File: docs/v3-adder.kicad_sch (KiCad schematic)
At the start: 102 parts, among them J1 Thonkiconn, J2 Thonkiconn, J3 Thonkiconn, J4 Thonkiconn, J5 Thonkiconn, J6 Thonkiconn, J7 Thonkiconn, J8 Thonkiconn, P1 Eurorack 2x5, SW1A SUBMINI ON-OFF-ON, SW1B SUBMINI ON-ON, SW2A SUBMINI ON-OFF-ON, SW2B SUBMINI ON-ON-ON, SW3A SUBMINI ON-OFF-ON, SW3B SUBMINI ON-ON-ON, SW4A SUBMINI ON-OFF-ON, SW4B SUBMINI ON-ON-ON, U1 OPA4196, U2 OPA4196, U3 OPA4196, U4 L78L05, U5 L79L05

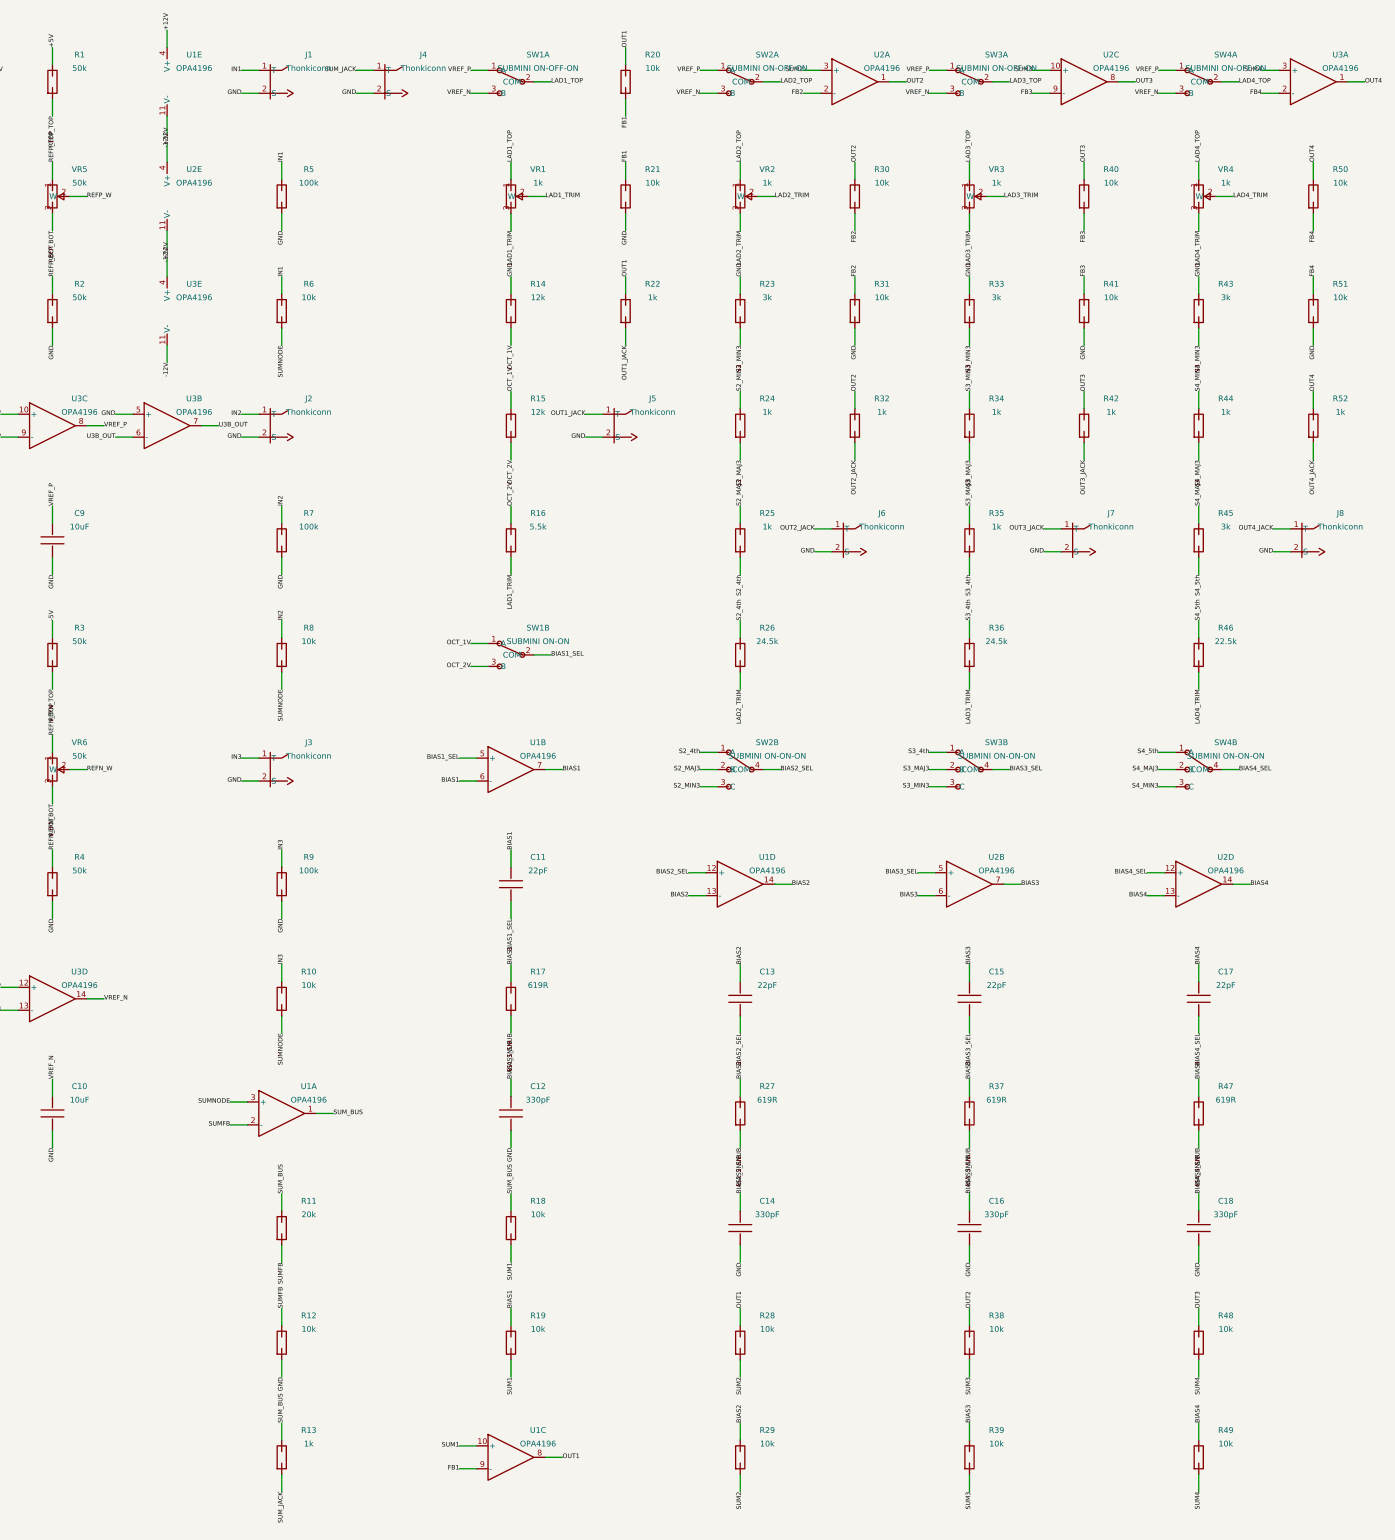
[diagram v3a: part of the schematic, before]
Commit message: Schematic: fix three functional defects found reviewing it
Asked to verify the schematic does what v3 needs before layout. The structure
was right - three summed inputs to SUM, four cascaded stages of polarity switch
plus tap selector plus buffer plus gain-2 adder, no leftover v2.2 passthru
buffers - but three things were wrong.

1. Unpatched inputs did not sum to zero. Each input jack had a 100k pulldown,
   which puts 110k rather than a driven 0 V on that leg of the passive
   averager. With one input patched - the normal case - the summer's gain was
   2.538 instead of 1.0, so a 1V/oct signal came out transposed by over an
   octave and a half. Fixed by wiring the Thonkiconn's own switch contact to
   GND, which grounds an unused tip properly; the pulldowns are gone.

2. No local decoupling on the op-amp packages. Only bulk caps at the power
   entry and the regulators. Added 0.1uF per rail per package, as v2.2 has.

3. A 22pF cap sat between each bias buffer's output and its + input, which is
   positive feedback around a follower. That was mine, not inherited: v2.2 puts
   its 22pF across the follower's feedback, and since that feedback is a plain
   wire the cap does nothing at all. Removed rather than reproduced.

check_function() now asserts the properties behind all three, plus the summing
ratios and the gain networks - things a connectivity check cannot see, because
a wrong value still connects. Verified against injected faults.

Still open before layout: the ON-ON-ON selectors are drawn as an ideal 1P3T,
but the physical part is a six-pin DPDT whose three positions come from
combining poles, and Type 1 and Type 2 differ. Symbol, footprint and tap wiring
all follow from which variant is bought.

ERC still 0 errors, 23 footprint warnings on the custom parts.

Co-Authored-By: Claude Opus 5 <noreply@anthropic.com>
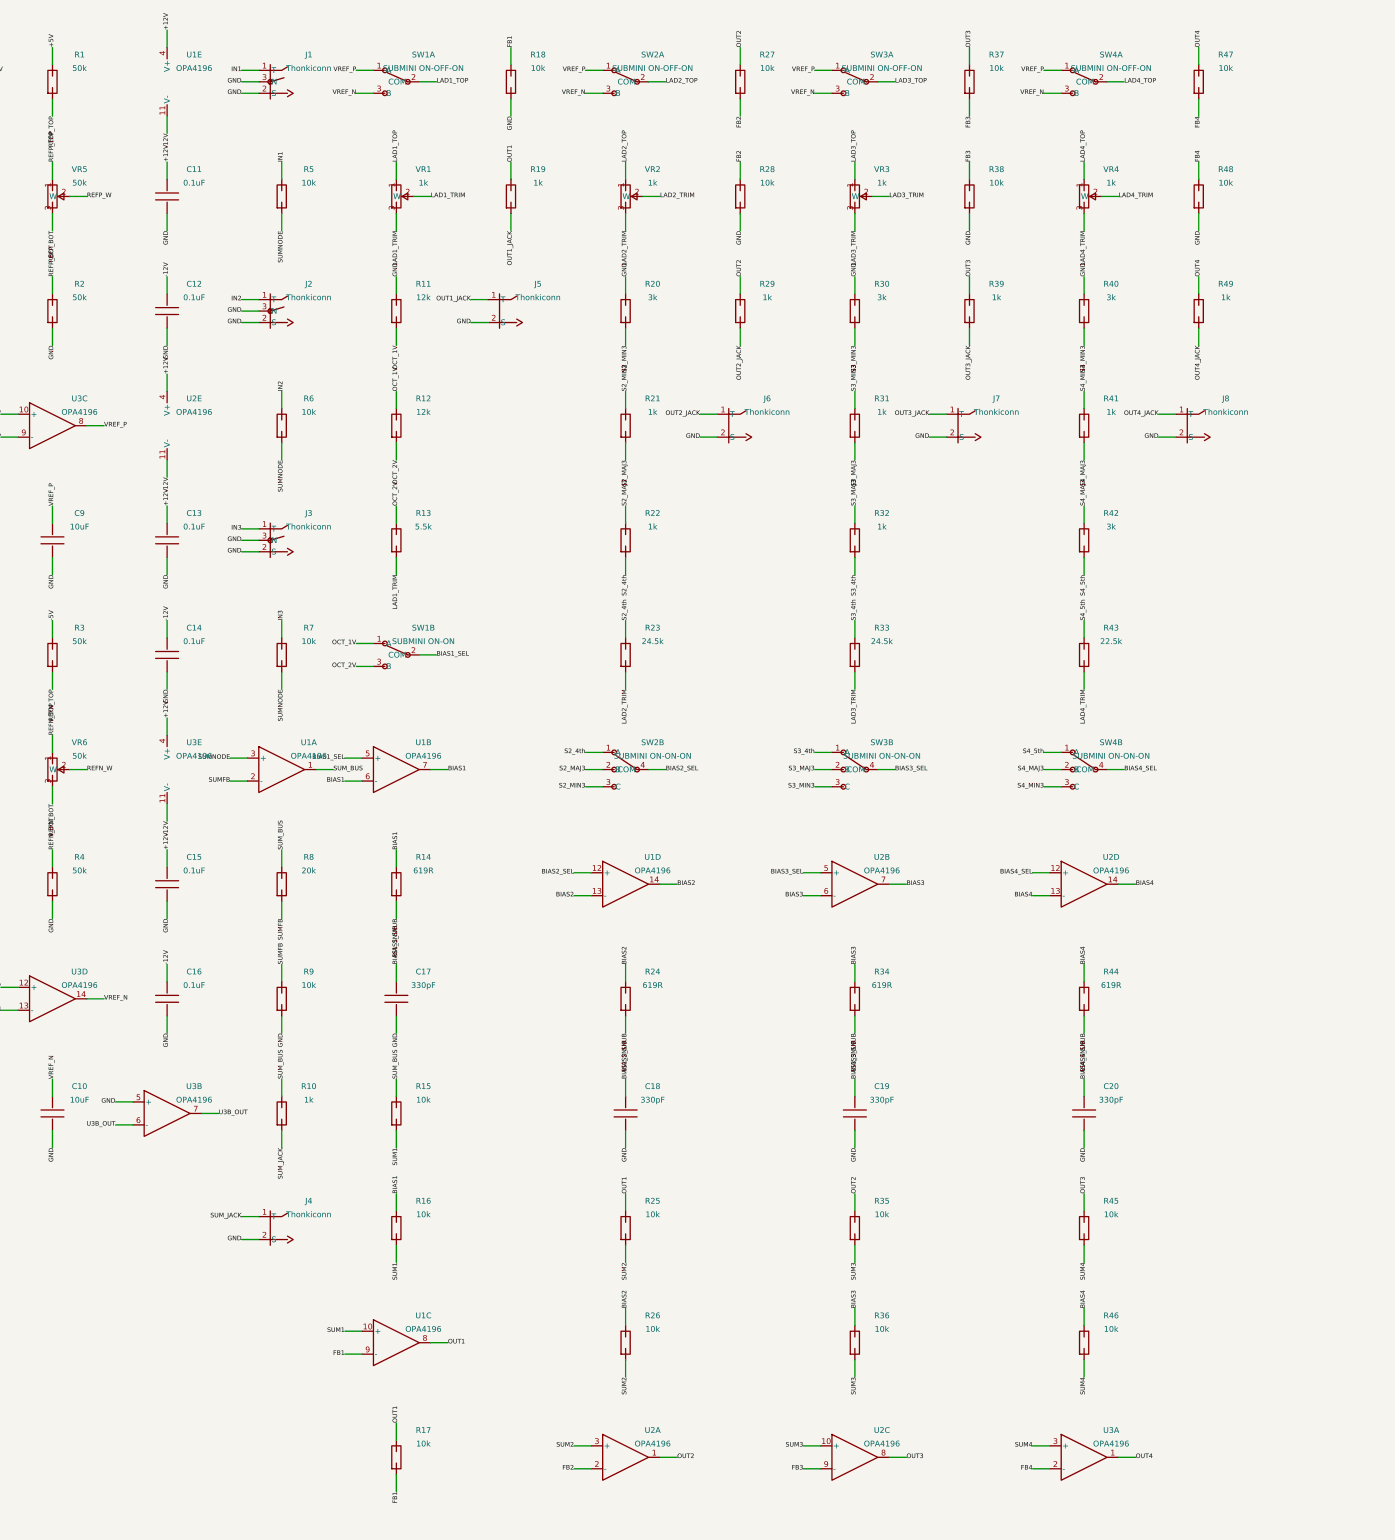
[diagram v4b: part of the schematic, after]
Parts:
- removed C11, C17: 22pF, Capacitor_SMD:C_0805_2012Metric, symbol adder:C
- removed C12: 330pF, Capacitor_SMD:C_0805_2012Metric, symbol adder:C
- removed J1, J2: Thonkiconn, THONKICONN-TIGHT, symbol adder:JACK
- removed R14: 12k, Resistor_SMD:R_0805_2012Metric, symbol adder:R
- removed R17, R27, R37: 619R, Resistor_SMD:R_0805_2012Metric, symbol adder:R
- removed R18, R20, R21, R30, R31, R40, R8: 10k, Resistor_SMD:R_0805_2012Metric, symbol adder:R
- removed R24, R25, R34: 1k, Resistor_SMD:R_0805_2012Metric, symbol adder:R
- removed R43: 3k, Resistor_SMD:R_0805_2012Metric, symbol adder:R
- added C13, C16: 0.1uF, Capacitor_SMD:C_0805_2012Metric, symbol adder:C
- added J2, J3: Thonkiconn, THONKICONN-TIGHT, symbol adder:JACK_SW
- added J5, J6: Thonkiconn, THONKICONN-TIGHT, symbol adder:JACK
- added R19: 1k, Resistor_SMD:R_0805_2012Metric, symbol adder:R
- added R26: 10k, Resistor_SMD:R_0805_2012Metric, symbol adder:R
- added SW1A, SW2A, SW3A, SW4A: SUBMINI ON-OFF-ON, SUBMINI_TOGGLE, symbol adder:SW_ONOFFON
- added SW3B, SW4B: SUBMINI ON-ON-ON, SUBMINI_TOGGLE, symbol adder:SW_1P3T
- added unit 3 of U1
- added unit 1 of U2
- added unit 3 of U2
- added unit 5 of U3
- added unit 2 of U3
- C11: renamed from U2; value OPA4196 -> 0.1uF; footprint Package_SO:SOIC-14_3.9x8.7mm_P1.27mm -> Capacitor_SMD:C_0805_2012Metric; symbol adder:OPA4196 -> adder:C
- C12: renamed from U3; value OPA4196 -> 0.1uF; footprint Package_SO:SOIC-14_3.9x8.7mm_P1.27mm -> Capacitor_SMD:C_0805_2012Metric; symbol adder:OPA4196 -> adder:C
- C14: value 330pF -> 0.1uF
- C15: value 22pF -> 0.1uF
- C17: renamed from U1; value OPA4196 -> 330pF; footprint Package_SO:SOIC-14_3.9x8.7mm_P1.27mm -> Capacitor_SMD:C_0805_2012Metric; symbol adder:OPA4196 -> adder:C
- C18: renamed from R29; value 10k -> 330pF; footprint Resistor_SMD:R_0805_2012Metric -> Capacitor_SMD:C_0805_2012Metric; symbol adder:R -> adder:C
- C19: renamed from R38; value 10k -> 330pF; footprint Resistor_SMD:R_0805_2012Metric -> Capacitor_SMD:C_0805_2012Metric; symbol adder:R -> adder:C
- J1: renamed from J3; symbol adder:JACK -> adder:JACK_SW
- J7: renamed from SW4A; value SUBMINI ON-OFF-ON -> Thonkiconn; footprint SUBMINI_TOGGLE -> THONKICONN-TIGHT; symbol adder:SW_ONOFFON -> adder:JACK
- R10: value 10k -> 1k
- R11: value 20k -> 12k
- R12: value 10k -> 12k
- R13: value 1k -> 5.5k
- R14: renamed from R19; value 10k -> 619R
- R15: value 12k -> 10k
- R16: value 5.5k -> 10k
- R17: renamed from J5; value Thonkiconn -> 10k; footprint THONKICONN-TIGHT -> Resistor_SMD:R_0805_2012Metric; symbol adder:JACK -> adder:R
- R18: renamed from SW2A; value SUBMINI ON-OFF-ON -> 10k; footprint SUBMINI_TOGGLE -> Resistor_SMD:R_0805_2012Metric; symbol adder:SW_ONOFFON -> adder:R
- R20: renamed from R26; value 24.5k -> 3k
- R21: renamed from SW2B; value SUBMINI ON-ON-ON -> 1k; footprint SUBMINI_TOGGLE -> Resistor_SMD:R_0805_2012Metric; symbol adder:SW_1P3T -> adder:R
- R23, R33: value 3k -> 24.5k
- R24: renamed from R28; value 10k -> 619R
- R25, R36: renamed from U2; value OPA4196 -> 10k; footprint Package_SO:SOIC-14_3.9x8.7mm_P1.27mm -> Resistor_SMD:R_0805_2012Metric; symbol adder:OPA4196 -> adder:R
- R27: renamed from R32; value 1k -> 10k
- R28: renamed from J6; value Thonkiconn -> 10k; footprint THONKICONN-TIGHT -> Resistor_SMD:R_0805_2012Metric; symbol adder:JACK -> adder:R
- R29: renamed from SW3A; value SUBMINI ON-OFF-ON -> 1k; footprint SUBMINI_TOGGLE -> Resistor_SMD:R_0805_2012Metric; symbol adder:SW_ONOFFON -> adder:R
- R30: renamed from R35; value 1k -> 3k
- R31: renamed from R36; value 24.5k -> 1k
- R32: renamed from SW3B; value SUBMINI ON-ON-ON -> 1k; footprint SUBMINI_TOGGLE -> Resistor_SMD:R_0805_2012Metric; symbol adder:SW_1P3T -> adder:R
- R34: renamed from C16; value 330pF -> 619R; footprint Capacitor_SMD:C_0805_2012Metric -> Resistor_SMD:R_0805_2012Metric; symbol adder:C -> adder:R
- R38: renamed from R42; value 1k -> 10k
- R39: renamed from J7; value Thonkiconn -> 1k; footprint THONKICONN-TIGHT -> Resistor_SMD:R_0805_2012Metric; symbol adder:JACK -> adder:R
- R40: renamed from R44; value 1k -> 3k
- R41: renamed from R45; value 3k -> 1k
- R42: renamed from R46; value 22.5k -> 3k
- R43: renamed from SW4B; value SUBMINI ON-ON-ON -> 22.5k; footprint SUBMINI_TOGGLE -> Resistor_SMD:R_0805_2012Metric; symbol adder:SW_1P3T -> adder:R
- R5, R7, R9: value 100k -> 10k
- R8: renamed from SW1A; value SUBMINI ON-OFF-ON -> 20k; footprint SUBMINI_TOGGLE -> Resistor_SMD:R_0805_2012Metric; symbol adder:SW_ONOFFON -> adder:R
- SW2B: renamed from C13; value 22pF -> SUBMINI ON-ON-ON; footprint Capacitor_SMD:C_0805_2012Metric -> SUBMINI_TOGGLE; symbol adder:C -> adder:SW_1P3T
- renumbered C18 to C20, R39 to R35, R41 to R37, R47 to R44, R48 to R45, R49 to R46, R50 to R47, R51 to R48, R52 to R49, U3 to U2
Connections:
- net +12V: now also C11.1, C15.1, U2.4 (V+), C13.1, U3.4 (V+); no longer C11.4 (V+), C12.4 (V+)
- net -12V: now also C12.1, C14.1, U2.11 (V-), C16.1, U3.11 (V-); no longer C11.11 (V-), C12.11 (V-)
- net BIAS1: now also R16.1
- net BIAS1_SNUB: now also C17.1, R14.2
- net BIAS2: now also R24.1, R26.1; no longer C18.1, SW2B.1
- net BIAS2_SEL: now also SW2B.4 (COM); no longer R21.4 (COM), SW2B.2
- net BIAS2_SNUB: now also C18.1, R24.2; no longer C14.1
- net BIAS3: now also R34.1, R36.1; no longer C15.1, R35.1
- net BIAS3_SEL: now also SW3B.4 (COM); no longer C15.2, R32.4 (COM)
- net BIAS3_SNUB: now also C19.1, R34.2; no longer R34.1
- net BIAS4_SEL: now also SW4B.4 (COM); no longer R43.4 (COM)
- net FB1: now also R17.2, R18.1, U1.9 (-); no longer C17.9 (-)
- net FB2: now also R27.2, R28.1, U2.2 (-); no longer R25.2 (-)
- net FB3: now also R37.2, R38.1, U2.9 (-); no longer R36.9 (-), R37.1
- net GND: now also C11.2, C12.2, C15.2, C17.2, C18.2, C19.2, J1.3 (N), J7.2 (S), R11.1, R18.2, R20.1, R30.1, R38.2, R40.1, C13.2, C16.2, J2.2 (S), J2.3 (N), J3.2 (S), J3.3 (N), J5.2 (S), J6.2 (S), U3.5 (+); no longer R12.2, R17.2 (S), R23.1, R33.1, R34.2, R37.2, R39.2 (S), R5.2, R7.2, U2.5 (+)
- net IN1: now also J1.1 (T); no longer R6.1
- net IN2: now also R6.1, J2.1 (T); no longer R7.1
- net IN3: now also R7.1, J3.1 (T); no longer J1.1 (T), R10.1, R9.1
- net LAD1_TOP: now also SW1A.2 (COM); no longer R8.2 (COM)
- net LAD1_TRIM: now also R13.2; no longer R16.2
- net LAD2_TOP: now also SW2A.2 (COM); no longer R18.2 (COM)
- net LAD2_TRIM: now also R23.2; no longer R20.2
- net LAD3_TOP: now also SW3A.2 (COM); no longer R29.2 (COM)
- net LAD3_TRIM: now also R33.2; no longer R31.2
- net LAD4_TOP: now also SW4A.2 (COM); no longer J7.2 (COM)
- net LAD4_TRIM: now also R43.2; no longer R42.2
- net OCT_1V: now also R11.2, R12.1; no longer R15.1
- net OCT_2V: now also R12.2, R13.1; no longer R15.2, R16.1
- net OUT1: now also R17.1, R25.1, R19.1, U1.8; no longer C17.8, R22.1, R24.1
- net OUT1_JACK: now also J5.1 (T), R19.2; no longer R17.1 (T), R22.2
- net OUT2: now also R29.1, R35.1, U2.1; no longer C19.1, R25.1
- net OUT2_JACK: now also R29.2, J6.1 (T); no longer R27.2, R28.1 (T)
- net OUT3: now also R37.1, R39.1, U2.8; no longer R36.8, R38.1
- net OUT3_JACK: now also J7.1 (T), R39.2; no longer R38.2, R39.1 (T)
- net S2_4th: now also R22.2, R23.1, SW2B.1 (A); no longer R20.1, R21.1 (A)
- net S2_MAJ3: now also R22.1, SW2B.2 (B)
- net S2_MIN3: now also R20.2, R21.1, SW2B.3 (C); no longer R21.3 (C), R23.2
- net S3_4th: now also R32.2, R33.1, SW3B.1 (A); no longer R30.2, R31.1, R32.1 (A)
- net S3_MAJ3: now also R31.2, R32.1, SW3B.2 (B); no longer R30.1, R32.2 (B)
- net S3_MIN3: now also R30.2, R31.1, SW3B.3 (C); no longer R32.3 (C), R33.2
- net S4_5th: now also R42.2, SW4B.1 (A); no longer R41.2, R42.1
- net S4_MAJ3: now also R41.2, R42.1, SW4B.2 (B); no longer R40.2, R41.1, R43.2 (B)
- net S4_MIN3: now also R40.2, R41.1, SW4B.3 (C); no longer R40.1, R43.3 (C)
- net SUM1: now also R15.2, R16.2, U1.10 (+); no longer C17.10 (+), R14.2
- net SUM2: now also R25.2, R26.2, U2.3 (+); no longer C18.2, R24.2, R25.3 (+)
- net SUM3: now also R36.2, U2.10 (+); no longer C19.2, R36.10 (+)
- net SUMFB: now also R8.2, R9.1; no longer R11.2, R12.1
- net SUMNODE: now also R5.2, R7.2; no longer R10.2
- net SUM_BUS: now also R10.1, R15.1, R8.1; no longer R11.1, R13.1
- net SUM_JACK: now also R10.2; no longer R13.2
- net U3B_OUT: now also U3.6 (-), U3.7; no longer U2.6 (-), U2.7
- net VREF_N: now also SW1A.3 (B), SW2A.3 (B), SW3A.3 (B), SW4A.3 (B); no longer J7.3 (B), R18.3 (B), R29.3 (B), R8.3 (B)
- net VREF_P: now also SW1A.1 (A), SW2A.1 (A), SW3A.1 (A), SW4A.1 (A); no longer J7.1 (A), R18.1 (A), R29.1 (A), R8.1 (A)
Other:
- moved on the sheet: C20, J8, R14, R20, R24, R27, R30, R31, R35, R37, R38, R40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
